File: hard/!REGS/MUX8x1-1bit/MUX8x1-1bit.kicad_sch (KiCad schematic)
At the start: 22 parts, among them J1 Conn_01x01_Male, J10 Conn_01x01_Male, J11 Conn_01x01_Male, J12 Conn_01x03_Male, J13 Conn_01x01_Male, J14 Conn_01x01_Male, J15 Conn_01x01_Male, J16 Conn_01x01_Male, J2 Conn_01x01_Male, J3 Conn_01x01_Male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

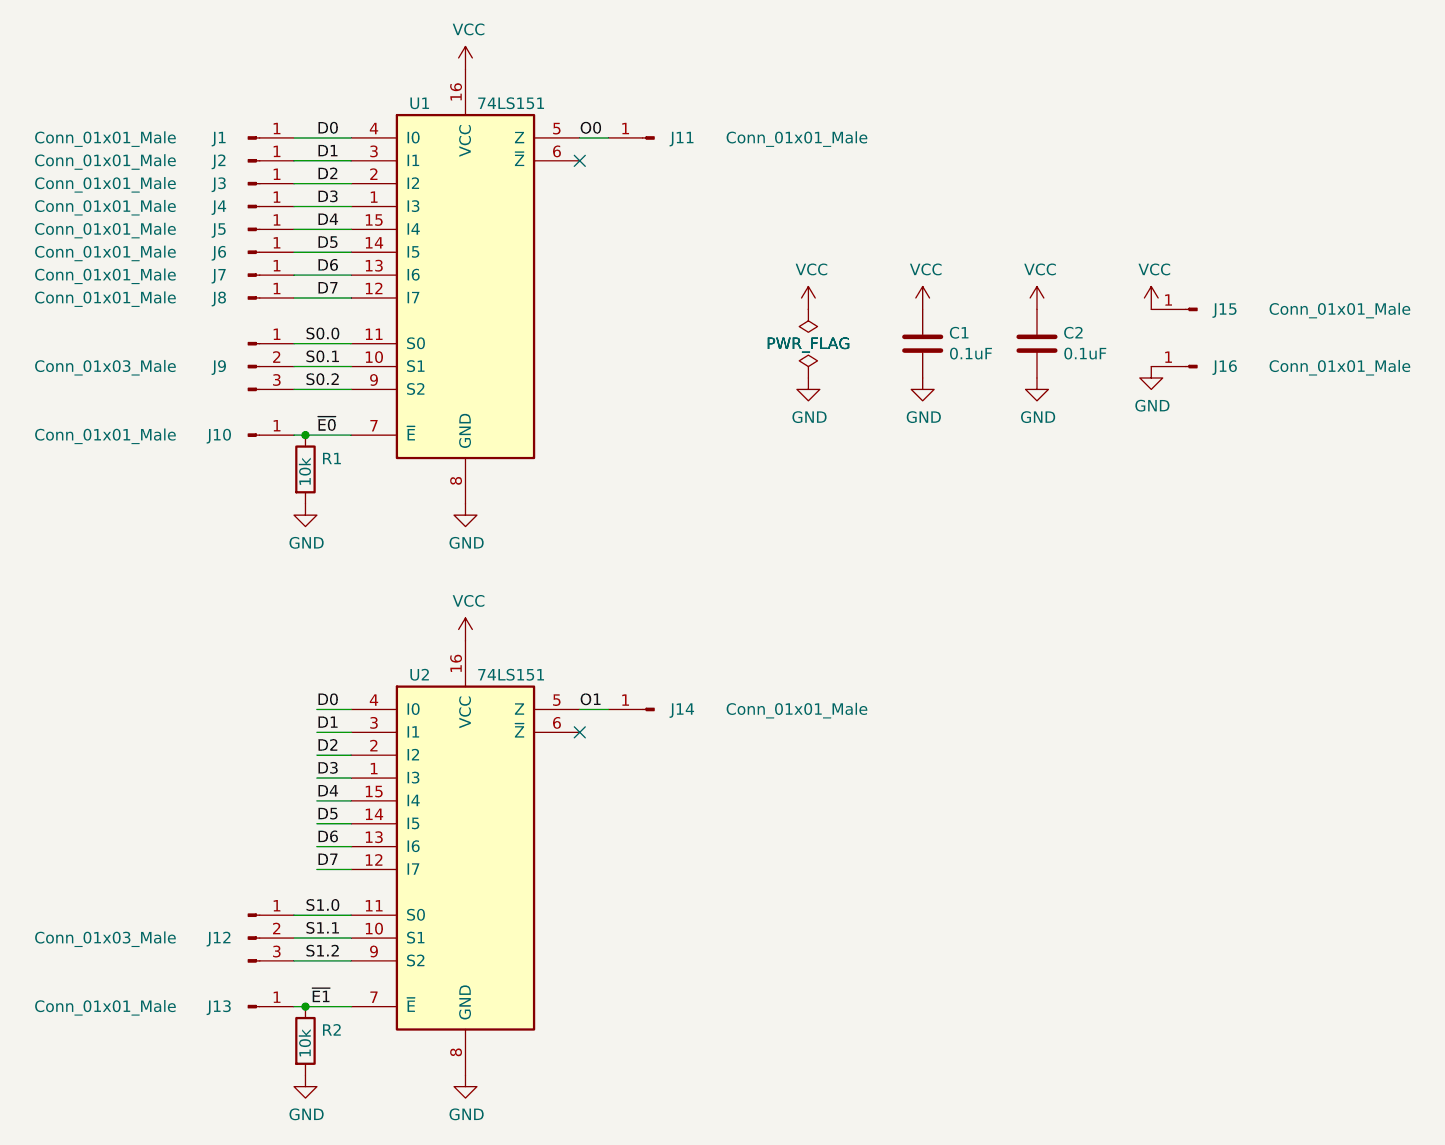
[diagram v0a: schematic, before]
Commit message: MUX8x1-1bit v2 rework
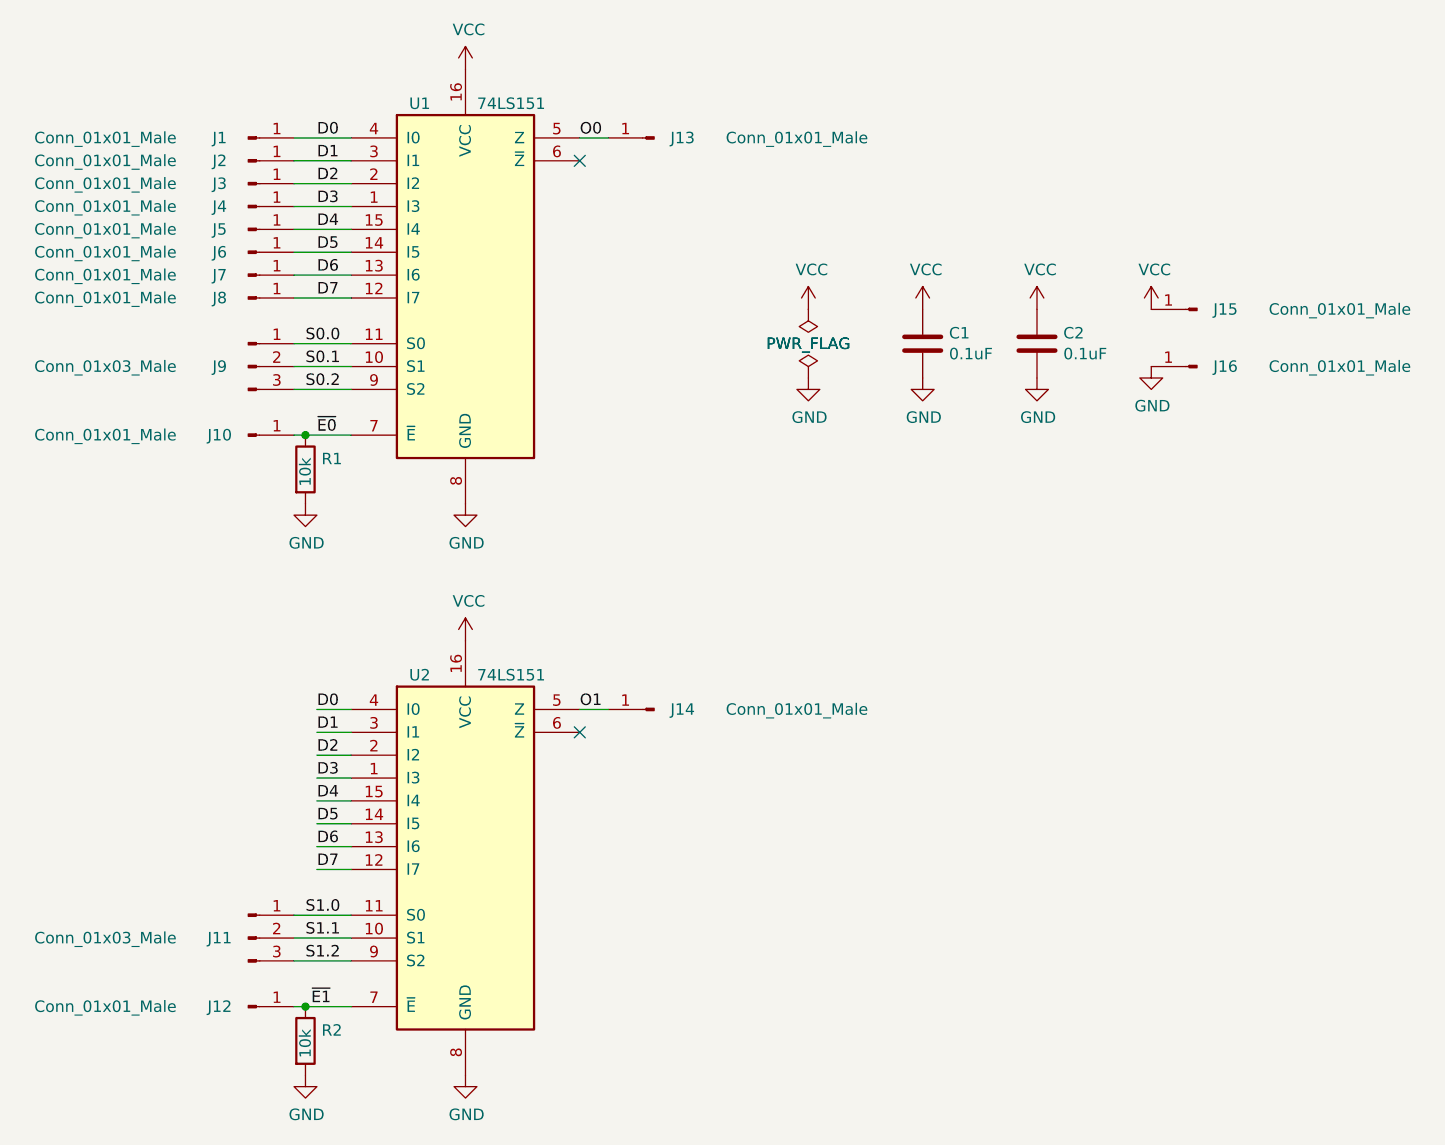
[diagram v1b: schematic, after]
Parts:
- renumbered J12 to J11, J13 to J12, J11 to J13
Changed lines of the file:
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@@
 		(on_board yes)
 		(dnp no)
-		(property "Reference" "J11"
+		(property "Reference" "J13"
 			(at 125.73 44.45 0)
 			(effects
@@
 			(project ""
 				(path "/59136139-153a-49f3-b23d-b591293b169a"
-					(reference "J11")
+					(reference "J13")
 					(unit 1)
 				)
@@
 		(on_board yes)
 		(dnp no)
-		(property "Reference" "J12"
+		(property "Reference" "J11"
 			(at 74.295 133.35 0)
 			(effects
@@
 			(project ""
 				(path "/59136139-153a-49f3-b23d-b591293b169a"
-					(reference "J12")
+					(reference "J11")
 					(unit 1)
 				)
@@
 		(on_board yes)
 		(dnp no)
-		(property "Reference" "J13"
+		(property "Reference" "J12"
 			(at 74.295 140.97 0)
 			(effects
@@
 			(project ""
 				(path "/59136139-153a-49f3-b23d-b591293b169a"
-					(reference "J13")
-					(unit 1)
-				)
+					(reference "J12")
+					(unit 1)
+				)
